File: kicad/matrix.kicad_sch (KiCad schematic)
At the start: 88 parts, among them SW1 Esc, SW10 F9, SW100 Down, SW101 Right, SW11 F10, SW12 F11, SW13 F12, SW14 PrintScreen, SW15 ScrollLock, SW16 PauseBreak, SW18 1, SW19 2, SW2 F1, SW20 3, SW21 4, SW22 5, SW23 6, SW24 7, SW25 8, SW26 9, SW27 0, SW28 -, SW29 =, SW3 F2, SW30 Backspace, SW31 Backspace, SW32 Insert, SW33 Home, SW34 PgUp, SW35 Tab, SW36 Q, SW37 W, SW38 E, SW39 R, SW4 F3, SW40 T, SW41 Y, SW42 U, SW43 I, SW44 O, SW45 P, SW46 [, SW47 ], SW48 \, SW5 F4, SW50 Delete, SW51 End, SW52 PgDw, SW53 CapsLock, SW54 A, SW55 S, SW56 D, SW57 F, SW58 G, SW59 H, SW6 F5, SW60 J, SW61 K, SW62 L, SW63 ;, SW64 ', SW65 \ ISO, SW66 Enter, SW68 Shift, SW69 \ ISO, SW7 F6, SW70 Z, SW71 X, SW72 C, SW73 V, SW74 B, SW75 N, SW76 M, SW77 ,, SW78 ., SW79 /, SW8 F7, SW80 Shift (???), SW81 Shift, SW83 Up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

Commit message: matrix update
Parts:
- added D1, D10, D11, D12, D13, D14, D15, D16, D17, D18, D19, D2, D20, D21, D22, D23, D24, D25, D26, D27, D28, D29, D3, D30, D31, D32, D33, D34, D35, D36, D37, D38, D39, D4, D40, D41, D42, D43, D44, D45, D46, D47, D48, D49, D5, D50, D51, D52, D53, D54, D55, D56, D57, D58, D59, D6, D60, D61, D62, D63, D64, D65, D66, D67, D68, D69, D7, D70, D71, D72, D73, D74, D75, D76, D77, D78, D79, D8, D80, D81, D82, D83, D84, D85, D86, D87, D9: D_Small_Filled, symbol Device:D_Small_Filled
- SW65: renamed from SW68; value Shift -> LShift
- SW77: renamed from SW80; value Shift (???) -> RShift (???)
- SW78: renamed from SW81; value Shift -> RShift
- renumbered SW31 to SW30-1, SW32 to SW31, SW33 to SW32, SW34 to SW33, SW35 to SW34, SW36 to SW35, SW37 to SW36, SW38 to SW37, SW39 to SW38, SW40 to SW39, SW41 to SW40, SW42 to SW41, SW43 to SW42, SW44 to SW43, SW45 to SW44, SW46 to SW45, SW47 to SW46, SW48 to SW47, SW50 to SW48, SW51 to SW49, SW52 to SW50, SW53 to SW51, SW54 to SW52, SW55 to SW53, SW56 to SW54, SW57 to SW55, SW58 to SW56, SW59 to SW57, SW60 to SW58, SW61 to SW59, SW62 to SW60, SW63 to SW61, SW64 to SW62, SW65 to SW63, SW66 to SW64, SW69 to SW66, SW70 to SW67, SW71 to SW68, SW72 to SW69, SW73 to SW70, SW74 to SW71, SW75 to SW72, SW76 to SW73, SW77 to SW74, SW78 to SW75, SW79 to SW76, SW83 to SW79, SW84 to SW80, SW86 to SW81, SW90 to SW82, SW96 to SW83, SW98 to SW84, SW99 to SW85, SW100 to SW86, SW101 to SW87
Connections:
- net COL0: now also D1.1 (K), D10.1 (K), D11.1 (K), D12.1 (K), D13.1 (K), D14.1 (K), D15.1 (K), D16.1 (K), D2.1 (K), D3.1 (K), D4.1 (K), D5.1 (K), D6.1 (K), D7.1 (K), D8.1 (K), D9.1 (K)
- net COL1: now also D18.1 (K), D19.1 (K), D20.1 (K), D21.1 (K), D22.1 (K), D23.1 (K), D24.1 (K), D25.1 (K), D26.1 (K), D27.1 (K), D28.1 (K), D29.1 (K), D30.1 (K), D31.1 (K), D32.1 (K), D33.1 (K)
- net COL2: now also D34.1 (K), D35.1 (K), D36.1 (K), D37.1 (K), D38.1 (K), D39.1 (K), D40.1 (K), D41.1 (K), D42.1 (K), D43.1 (K), D44.1 (K), D45.1 (K), D46.1 (K), D47.1 (K), D48.1 (K), D49.1 (K), D50.1 (K)
- net COL3: now also D51.1 (K), D52.1 (K), D53.1 (K), D54.1 (K), D55.1 (K), D56.1 (K), D57.1 (K), D58.1 (K), D59.1 (K), D60.1 (K), D61.1 (K), D62.1 (K), D63.1 (K)
- net COL4: now also D65.1 (K), D66.1 (K), D67.1 (K), D68.1 (K), D69.1 (K), D70.1 (K), D71.1 (K), D72.1 (K), D73.1 (K), D74.1 (K), D75.1 (K), D76.1 (K), D77.1 (K), D78.1 (K), D79.1 (K)
- net COL5: now also D80.1 (K), D81.1 (K), D82.1 (K), D83.1 (K), D84.1 (K), D85.1 (K), D86.1 (K), D87.1 (K)
- net at SW85.1: now also D85.2 (A)
- net at SW14.1: now also D14.2 (A)
- net at SW16.1: now also D16.2 (A)
- net at SW80.1: now also D80.2 (A)
- net at SW24.1: now also D24.2 (A)
- net at SW20.1: now also D21.2 (A)
- net at SW15.1: now also D15.2 (A)
- net at SW44.1: now also D44.2 (A)
- net at SW42.1: now also D42.2 (A)
- net at SW68.1: now also D68.2 (A)
- net at SW81.1: now also D81.2 (A)
- net at SW70.1: now also D70.2 (A)
- net at SW34.1: now also D34.2 (A)
- net at SW41.1: now also D41.2 (A)
- net at SW43.1: now also D43.2 (A)
- net at SW67.1: now also D67.2 (A)
- net at SW52.1: now also D52.2 (A)
- net at SW17.1: now also D18.2 (A)
- net at SW45.1: now also D45.2 (A)
- net at SW84.1: now also D84.2 (A)
- net at SW22.1: now also D23.2 (A)
- net at SW72.1: now also D72.2 (A)
- net at SW64.1: now also D63.2 (A)
- net at SW82.1: now also D82.2 (A)
- net at SW32.1: now also D32.2 (A)
- net at SW61.1: now also D60.2 (A)
- net at SW79.1: now also D79.2 (A)
- net at SW57.1: now also D56.2 (A)
- net at SW75.1: now also D75.2 (A)
- net at SW13.1: now also D13.2 (A)
- net at SW33.1: now also D33.2 (A)
- net at SW4.1: now also D4.2 (A)
- net at SW29.1: now also D29.2 (A)
- net at SW55.1: now also D54.2 (A)
- net at SW39.1: now also D39.2 (A)
- net at SW78.1: now also D78.2 (A)
- net at SW36.1: now also D36.2 (A)
- net at SW49.1: now also D49.2 (A)
- net at SW48.1: now also D48.2 (A)
- net at SW31.1: now also D31.2 (A)
- net at SW3.1: now also D3.2 (A)
- net at SW54.1: now also D53.2 (A)
- net at SW9.1: now also D9.2 (A)
- net at SW8.1: now also D8.2 (A)
- net at SW83.1: now also D83.2 (A)
- net at SW63.1: now also D62.2 (A)
- net at SW7.1: now also D7.2 (A)
- net at SW73.1: now also D73.2 (A)
- net at SW40.1: now also D40.2 (A)
- net at SW51.1: now also D51.2 (A)
- net at SW69.1: now also D69.2 (A)
- net at SW59.1: now also D58.2 (A)
- net at SW30-1.1, SW30.1: now also D30.2 (A)
- net at SW12.1: now also D12.2 (A)
- net at SW86.1: now also D86.2 (A)
- net at SW66.1: now also D66.2 (A)
- net at SW56.1: now also D55.2 (A)
- net at SW65.1: now also D65.2 (A)
- net at SW62.1: now also D61.2 (A)
- net at SW71.1: now also D71.2 (A)
- net at SW37.1: now also D37.2 (A)
- net at SW25.1: now also D25.2 (A)
- net at SW27.1: now also D27.2 (A)
- net at SW18.1: now also D19.2 (A)
- net at SW77.1: now also D77.2 (A)
- net at SW26.1: now also D26.2 (A)
- net at SW2.1: now also D2.2 (A)
- net at SW6.1: now also D6.2 (A)
- net at SW21.1: now also D22.2 (A)
- net at SW11.1: now also D11.2 (A)
- net at SW35.1: now also D35.2 (A)
- net at SW76.1: now also D76.2 (A)
- net at SW74.1: now also D74.2 (A)
- net at SW47.1: now also D47.2 (A)
- net at SW38.1: now also D38.2 (A)
- net at SW87.1: now also D87.2 (A)
- net at SW10.1: now also D10.2 (A)
- net at SW46.1: now also D46.2 (A)
- net at SW28.1: now also D28.2 (A)
- net at SW60.1: now also D59.2 (A)
- net at SW1.1: now also D1.2 (A)
- net at SW5.1: now also D5.2 (A)
- net at SW58.1: now also D57.2 (A)
- net at SW19.1: now also D20.2 (A)
- net at SW50.1: now also D50.2 (A)
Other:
- moved on the sheet: SW1, SW10, SW11, SW12, SW13, SW14, SW15, SW16, SW17, SW18, SW19, SW2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

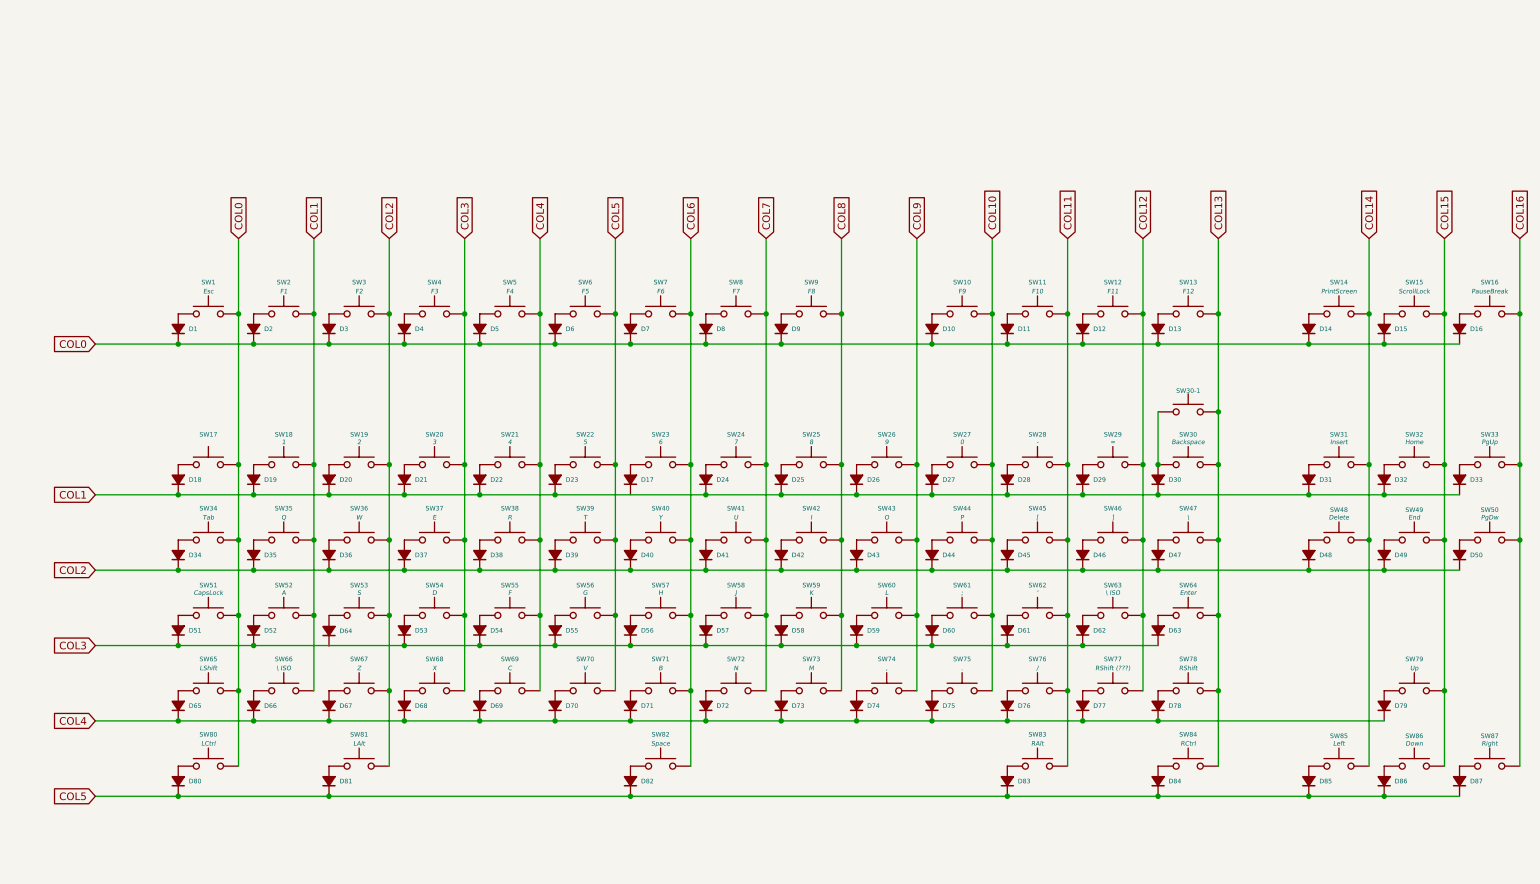
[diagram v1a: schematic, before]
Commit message: Add new symbols to schematic and update selection filter
Added symbols for MCP73831-2-OT, USB_C_Receptacle_USB2.0_14P, R_Small, and MDBT50Q-1MV2 to ibm-modern-m-ssk.kicad_sch. Updated selection filter in ibm-modern-m-ssk.kicad_prl to enable all item types. Removed an old backup zip and renamed a lock file.
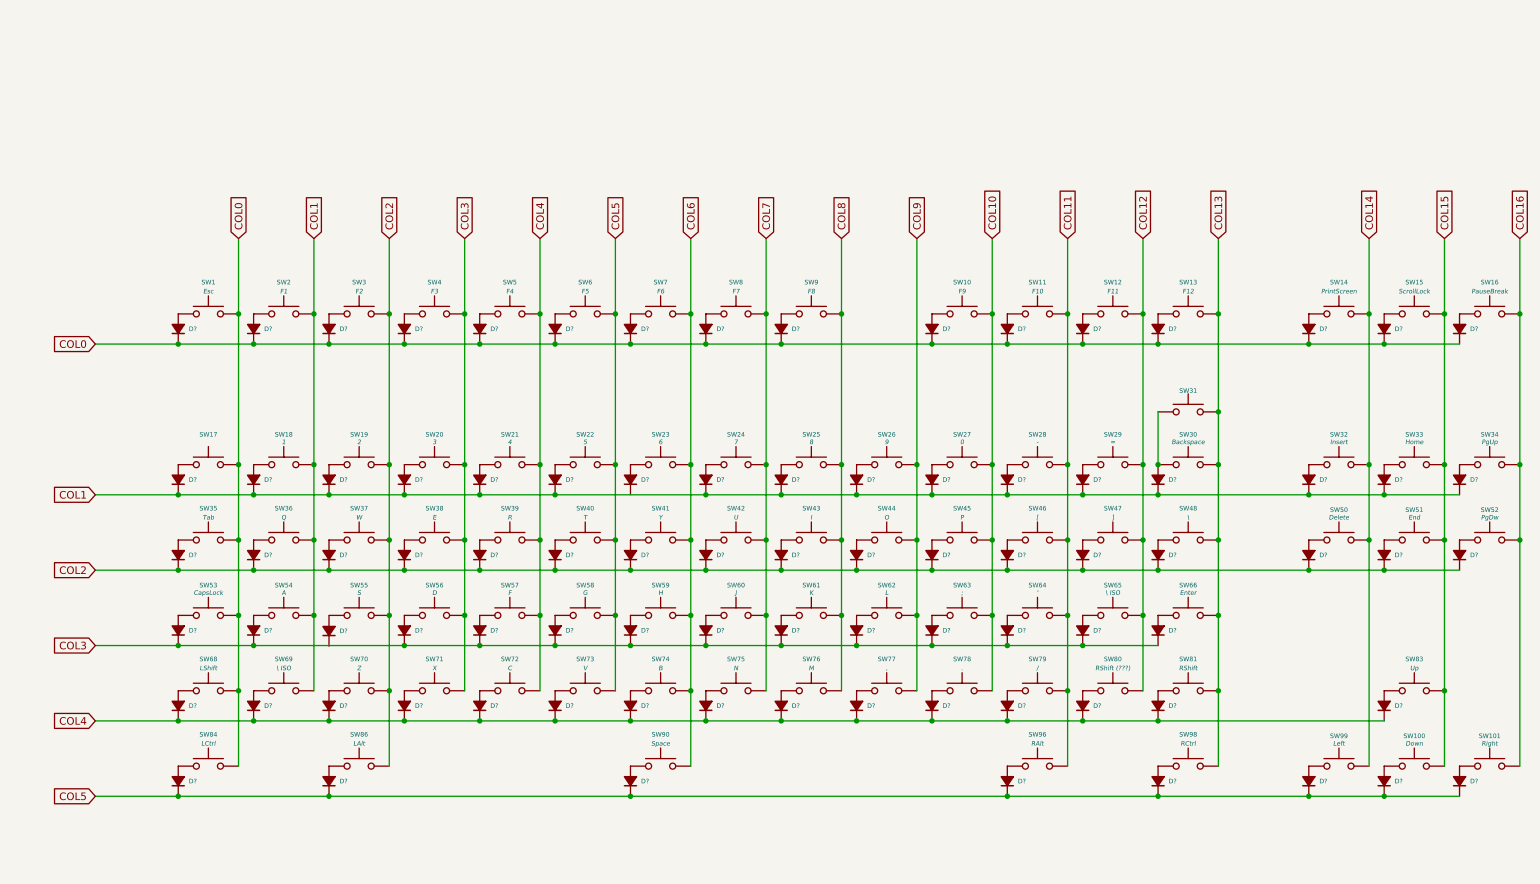
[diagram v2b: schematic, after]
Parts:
- renumbered D6 to D?, D78 to D?, D10 to D?, D32 to D?, D67 to D?, D29 to D?, D33 to D?, D25 to D?, D23 to D?, D11 to D?, D51 to D?, D5 to D?, D9 to D?, D41 to D?, D52 to D?, D59 to D?, D48 to D?, D87 to D?, D22 to D?, D12 to D?, D35 to D?, D4 to D?, D64 to D?, D81 to D?, D8 to D?, D43 to D?, D56 to D?, D54 to D?, D13 to D?, D77 to D?, D16 to D?, D47 to D?, D70 to D?, D20 to D?, D76 to D?, D36 to D?, D85 to D?, D38 to D?, D7 to D?, D80 to D?, D39 to D?, D58 to D?, D50 to D?, D73 to D?, D18 to D?, D31 to D?, D30 to D?, D44 to D?, D63 to D?, D26 to D?, D46 to D?, D17 to D?, D55 to D?, D74 to D?, D28 to D?, D45 to D?, D79 to D?, D37 to D?, D71 to D?, D49 to D?, D66 to D?, D83 to D?, D27 to D?, D68 to D?, D34 to D?, D57 to D?, D24 to D?, D72 to D?, D1 to D?, D19 to D?, D61 to D?, D53 to D?, D42 to D?, D65 to D?, D69 to D?, D15 to D?, D62 to D?, D82 to D?, D2 to D?, D75 to D?, D86 to D?, D84 to D?, D14 to D?, D40 to D?, D3 to D?, D60 to D?, D21 to D?, SW86 to SW100, SW87 to SW101, SW30-1 to SW31, SW31 to SW32, SW32 to SW33, SW33 to SW34, SW34 to SW35, SW35 to SW36, SW36 to SW37, SW37 to SW38, SW38 to SW39, SW39 to SW40, SW40 to SW41, SW41 to SW42, SW42 to SW43, SW43 to SW44, SW44 to SW45, SW45 to SW46, SW46 to SW47, SW47 to SW48, SW48 to SW50, SW49 to SW51, SW50 to SW52, SW51 to SW53, SW52 to SW54, SW53 to SW55, SW54 to SW56, SW55 to SW57, SW56 to SW58, SW57 to SW59, SW58 to SW60, SW59 to SW61, SW60 to SW62, SW61 to SW63, SW62 to SW64, SW63 to SW65, SW64 to SW66, SW65 to SW68, SW66 to SW69, SW67 to SW70, SW68 to SW71, SW69 to SW72, SW70 to SW73, SW71 to SW74, SW72 to SW75, SW73 to SW76, SW74 to SW77, SW75 to SW78, SW76 to SW79, SW77 to SW80, SW78 to SW81, SW79 to SW83, SW80 to SW84, SW81 to SW86, SW82 to SW90, SW83 to SW96, SW84 to SW98, SW85 to SW99

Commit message: Schematic Done v2
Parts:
- D10, D11, D12, D13, D14, D15, D16, D17, D18, D19, D20, D21, D22, D23, D24, D25, D26, D27, D28, D29, D30, D31, D32, D33, D34, D35, D36, D37, D38, D39, D40, D41, D42, D43, D44, D45, D46, D47, D48, D49, D5, D50, D51, D52, D53, D54, D55, D56, D57, D58, D59, D6, D60, D61, D62, D63, D64, D65, D66, D67, D68, D69, D7, D70, D71, D72, D73, D74, D75, D76, D77, D78, D79, D8, D80, D81, D82, D83, D84, D85, D86, D87, D88, D89, D9, D90, D91: renamed from D?; symbol Device:D_Small_Filled -> Device:D_Small
- renumbered SW31 to SW17, SW17 to SW18, SW18 to SW19, SW19 to SW20, SW20 to SW21, SW21 to SW22, SW22 to SW23, SW23 to SW24, SW24 to SW25, SW25 to SW26, SW26 to SW27, SW27 to SW28, SW28 to SW29, SW29 to SW30, SW30 to SW31, SW50 to SW49, SW51 to SW50, SW52 to SW51, SW53 to SW52, SW54 to SW53, SW55 to SW54, SW56 to SW55, SW57 to SW56, SW58 to SW57, SW59 to SW58, SW60 to SW59, SW61 to SW60, SW62 to SW61, SW63 to SW62, SW64 to SW63, SW65 to SW64, SW66 to SW65, SW68 to SW66, SW69 to SW67, SW70 to SW68, SW71 to SW69, SW72 to SW70, SW73 to SW71, SW74 to SW72, SW75 to SW73, SW76 to SW74, SW77 to SW75, SW78 to SW76, SW79 to SW77, SW80 to SW78, SW81 to SW79, SW83 to SW80, SW84 to SW81, SW86 to SW82, SW90 to SW83, SW96 to SW84, SW98 to SW85, SW99 to SW86, SW100 to SW87, SW101 to SW88

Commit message: Footprints & BOM done
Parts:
- D10, D11, D12, D13, D14, D15, D16, D17, D18, D19, D20, D21, D22, D23, D24, D25, D26, D27, D28, D29, D30, D31, D32, D33, D34, D35, D36, D37, D38, D39, D40, D41, D42, D43, D44, D45, D46, D47, D48, D49, D5, D50, D51, D52, D53, D54, D55, D56, D57, D58, D59, D6, D60, D61, D62, D63, D64, D65, D66, D67, D68, D69, D7, D70, D71, D72, D73, D74, D75, D76, D77, D78, D79, D8, D80, D81, D82, D83, D84, D85, D86, D87, D88, D89, D9, D90, D91: footprint (none) -> easyeda2kicad:SOD-723_L1.0-W0.6-P1.4-RD; LCSC Part (none) -> C2288
- SW1, SW10, SW11, SW12, SW13, SW14, SW15, SW16, SW17, SW18, SW19, SW2, SW20, SW21, SW22, SW23, SW24, SW25, SW26, SW27, SW28, SW29, SW3, SW30, SW31, SW32, SW33, SW34, SW35, SW36, SW37, SW38, SW39, SW4, SW40, SW41, SW42, SW43, SW44, SW45, SW46, SW47, SW48, SW49, SW5, SW50, SW51, SW52, SW53, SW54, SW55, SW56, SW57, SW58, SW59, SW6, SW60, SW61, SW62, SW63, SW64, SW65, SW66, SW67, SW68, SW69, SW7, SW70, SW71, SW72, SW73, SW74, SW75, SW76, SW77, SW78, SW79, SW8, SW80, SW81, SW82, SW83, SW84, SW85, SW86, SW87, SW88, SW9: footprint (none) -> ibm_bs:ibm_bs_1u; now left out of the parts list

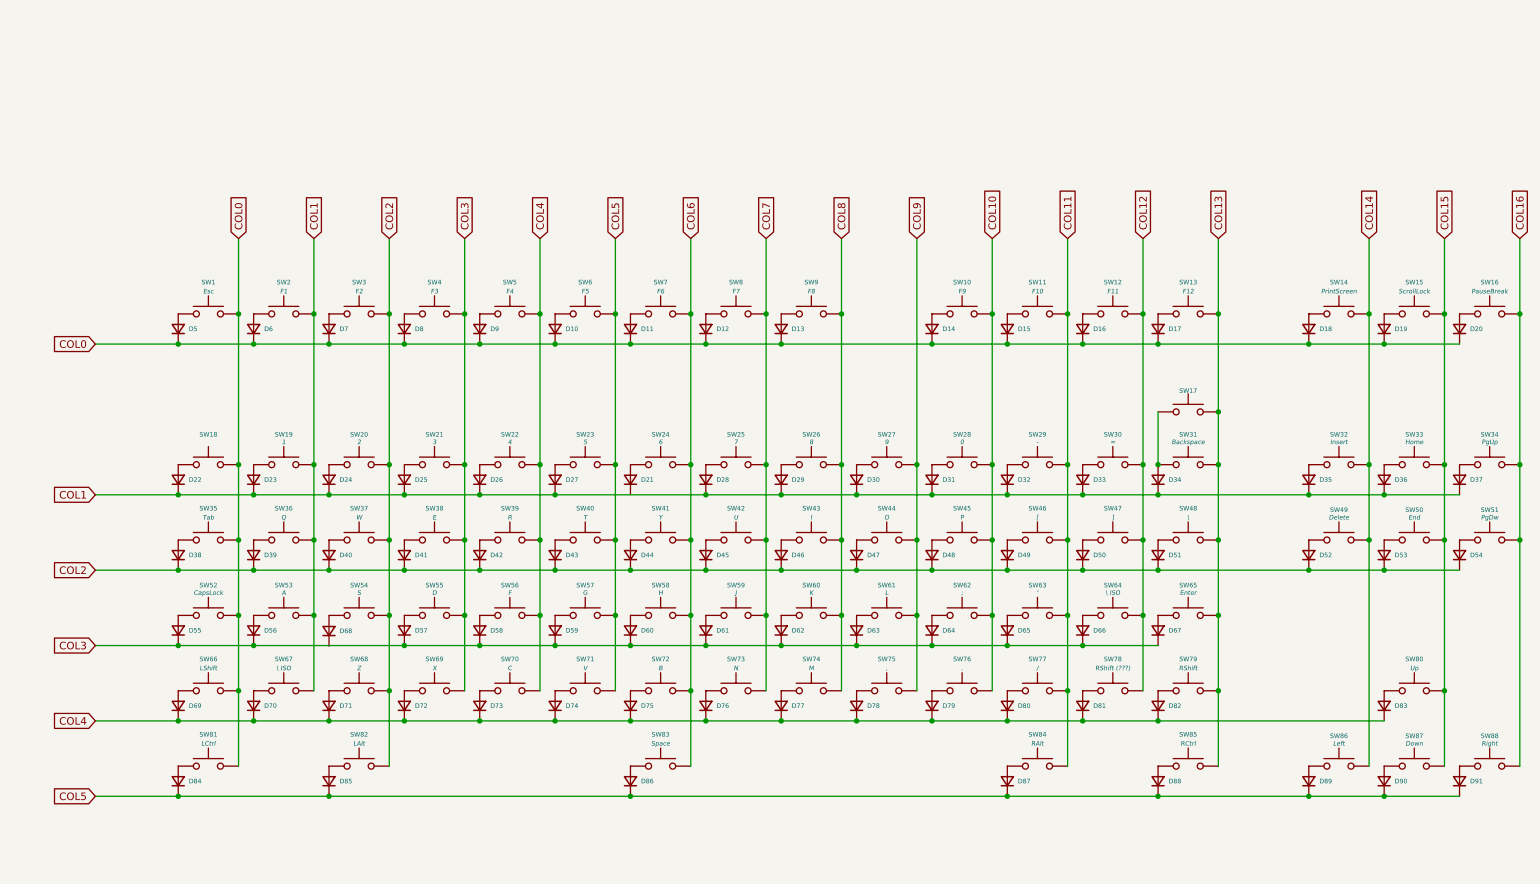
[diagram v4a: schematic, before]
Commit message: Update KiCad schematic, project files and backups
Rotate backups, and adjust KiCad project/schematic files. Deleted kicad/#auto_saved_files# and removed an old backup; added two new ibm-modern-m-ssk backup zips. Updated kicad/ibm-modern-m-ssk.kicad_prl and .kicad_pro (visible items/layers and meta/version changes, and removal of a netclass priority). Large edits to kicad/matrix.kicad_sch: added FPC connector symbol (TF38-24S-0.5SV), updated many component/junction coordinates and symbol details (likely placement/layout changes or library imports). Also renamed a .lck entry. These changes reflect schematic updates and housekeeping for project backups.
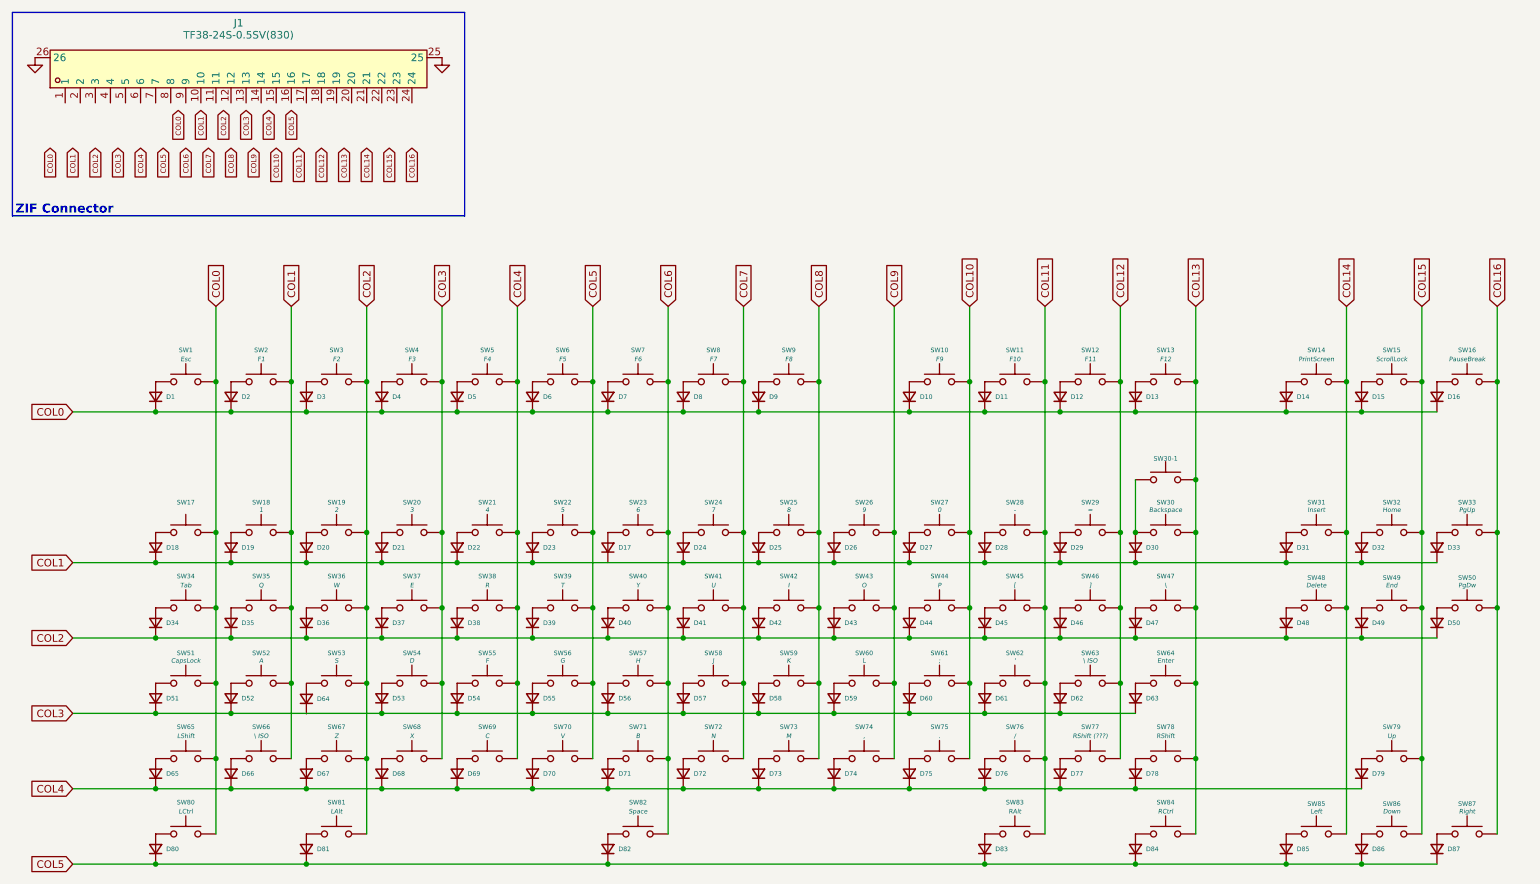
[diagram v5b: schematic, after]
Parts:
- added J1: TF38-24S-0.5SV(830), easyeda2kicad:FPC-SMD_24P-P0.50_TF38-24S-0.5SV-830, symbol easyeda2kicad:TF38-24S-0.5SV(830)
- renumbered D5 to D1, D14 to D10, D15 to D11, D16 to D12, D17 to D13, D18 to D14, D19 to D15, D20 to D16, D21 to D17, D22 to D18, D23 to D19, D6 to D2, D24 to D20, D25 to D21, D26 to D22, D27 to D23, D28 to D24, D29 to D25, D30 to D26, D31 to D27, D32 to D28, D33 to D29, D7 to D3, D34 to D30, D35 to D31, D36 to D32, D37 to D33, D38 to D34, D39 to D35, D40 to D36, D41 to D37, D42 to D38, D43 to D39, D8 to D4, D44 to D40, D45 to D41, D46 to D42, D47 to D43, D48 to D44, D49 to D45, D50 to D46, D51 to D47, D52 to D48, D53 to D49, D9 to D5, D54 to D50, D55 to D51, D56 to D52, D57 to D53, D58 to D54, D59 to D55, D60 to D56, D61 to D57, D62 to D58, D63 to D59, D10 to D6, D64 to D60, D65 to D61, D66 to D62, D67 to D63, D68 to D64, D69 to D65, D70 to D66, D71 to D67, D72 to D68, D73 to D69, D11 to D7, D74 to D70, D75 to D71, D76 to D72, D77 to D73, D78 to D74, D79 to D75, D80 to D76, D81 to D77, D82 to D78, D83 to D79, D12 to D8, D84 to D80, D85 to D81, D86 to D82, D87 to D83, D88 to D84, D89 to D85, D90 to D86, D91 to D87, D13 to D9, SW18 to SW17, SW19 to SW18, SW20 to SW19, SW21 to SW20, SW22 to SW21, SW23 to SW22, SW24 to SW23, SW25 to SW24, SW26 to SW25, SW27 to SW26, SW28 to SW27, SW29 to SW28, SW30 to SW29, SW31 to SW30, SW17 to SW30-1, SW32 to SW31, SW33 to SW32, SW34 to SW33, SW35 to SW34, SW36 to SW35, SW37 to SW36, SW38 to SW37, SW39 to SW38, SW40 to SW39, SW41 to SW40, SW42 to SW41, SW43 to SW42, SW44 to SW43, SW45 to SW44, SW46 to SW45, SW47 to SW46, SW48 to SW47, SW49 to SW48, SW50 to SW49, SW51 to SW50, SW52 to SW51, SW53 to SW52, SW54 to SW53, SW55 to SW54, SW56 to SW55, SW57 to SW56, SW58 to SW57, SW59 to SW58, SW60 to SW59, SW61 to SW60, SW62 to SW61, SW63 to SW62, SW64 to SW63, SW65 to SW64, SW66 to SW65, SW67 to SW66, SW68 to SW67, SW69 to SW68, SW70 to SW69, SW71 to SW70, SW72 to SW71, SW73 to SW72, SW74 to SW73, SW75 to SW74, SW76 to SW75, SW77 to SW76, SW78 to SW77, SW79 to SW78, SW80 to SW79, SW81 to SW80, SW82 to SW81, SW83 to SW82, SW84 to SW83, SW85 to SW84, SW86 to SW85, SW87 to SW86, SW88 to SW87
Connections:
- new net GND: J1.25, J1.26
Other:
- note added: "ZIF Connector"
- moved on the sheet: D1, D10, D11, D12, D13, D14, D15, D16, D17, D18, D19, D2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

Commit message: Add LiPo STEP/module and backups, update schematic
Add LiPo_603450_1200mAh STEP (3D) and corresponding .kicad_mod to the easyeda2kicad libraries, add two ibm-modern-m-ssk backup ZIPs, and update kicad/matrix.kicad_sch. Remove stale PCB lock file (~ibm-modern-m-ssk.kicad_pcb.lck). These changes introduce a battery 3D model/module and include recent project backups while applying a schematic update.
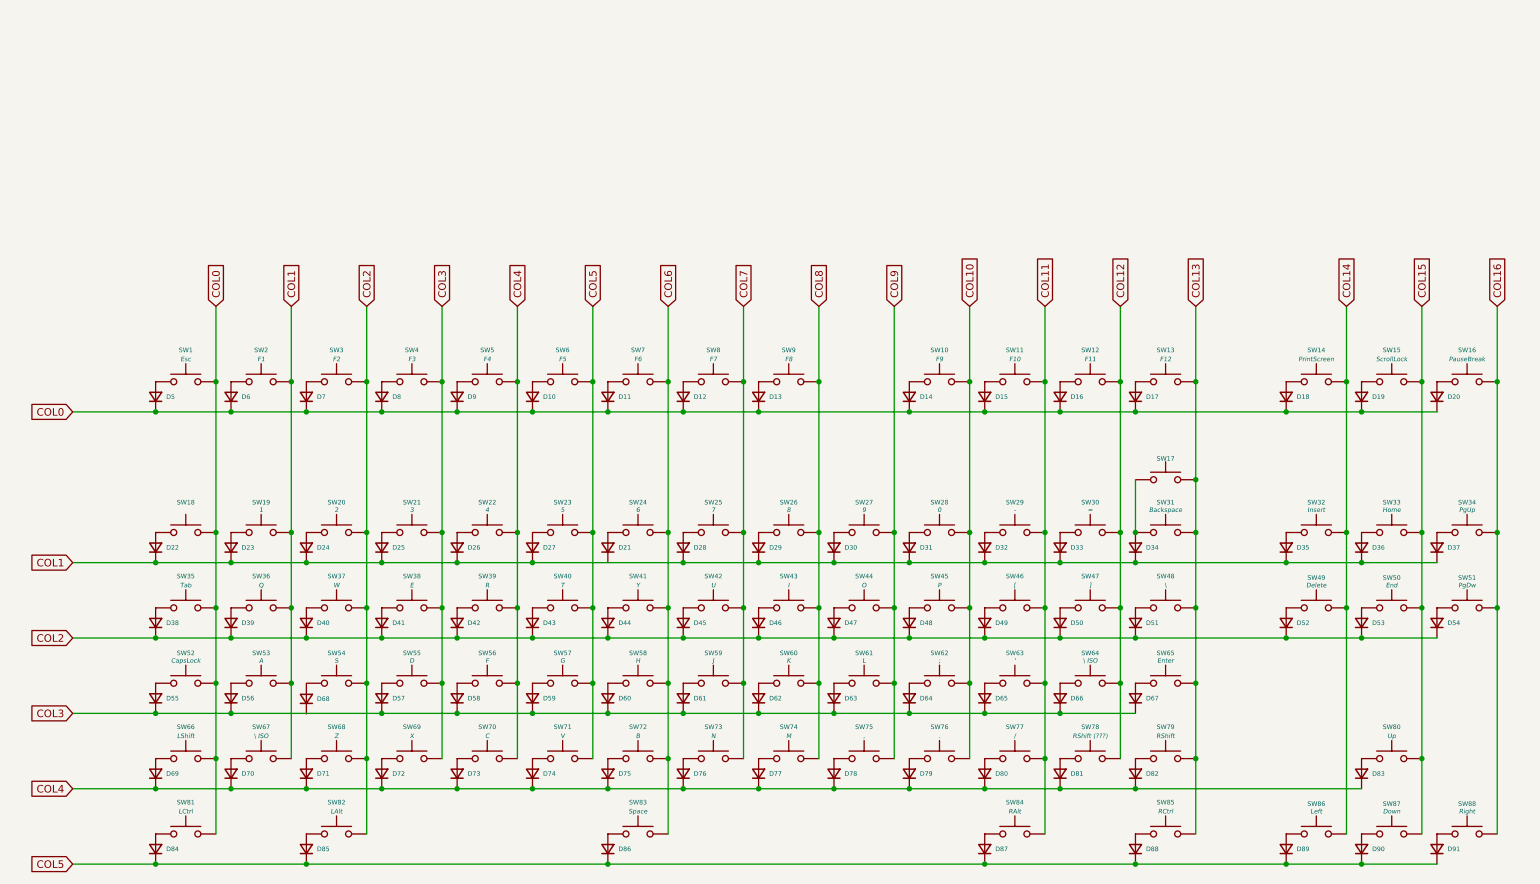
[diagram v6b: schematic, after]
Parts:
- removed J1: TF38-24S-0.5SV(830), easyeda2kicad:FPC-SMD_24P-P0.50_TF38-24S-0.5SV-830, symbol easyeda2kicad:TF38-24S-0.5SV(830)
- renumbered D6 to D10, D7 to D11, D8 to D12, D9 to D13, D10 to D14, D11 to D15, D12 to D16, D13 to D17, D14 to D18, D15 to D19, D16 to D20, D17 to D21, D18 to D22, D19 to D23, D20 to D24, D21 to D25, D22 to D26, D23 to D27, D24 to D28, D25 to D29, D26 to D30, D27 to D31, D28 to D32, D29 to D33, D30 to D34, D31 to D35, D32 to D36, D33 to D37, D34 to D38, D35 to D39, D36 to D40, D37 to D41, D38 to D42, D39 to D43, D40 to D44, D41 to D45, D42 to D46, D43 to D47, D44 to D48, D45 to D49, D1 to D5, D46 to D50, D47 to D51, D48 to D52, D49 to D53, D50 to D54, D51 to D55, D52 to D56, D53 to D57, D54 to D58, D55 to D59, D2 to D6, D56 to D60, D57 to D61, D58 to D62, D59 to D63, D60 to D64, D61 to D65, D62 to D66, D63 to D67, D64 to D68, D65 to D69, D3 to D7, D66 to D70, D67 to D71, D68 to D72, D69 to D73, D70 to D74, D71 to D75, D72 to D76, D73 to D77, D74 to D78, D75 to D79, D4 to D8, D76 to D80, D77 to D81, D78 to D82, D79 to D83, D80 to D84, D81 to D85, D82 to D86, D83 to D87, D84 to D88, D85 to D89, D5 to D9, D86 to D90, D87 to D91, SW30-1 to SW17, SW17 to SW18, SW18 to SW19, SW19 to SW20, SW20 to SW21, SW21 to SW22, SW22 to SW23, SW23 to SW24, SW24 to SW25, SW25 to SW26, SW26 to SW27, SW27 to SW28, SW28 to SW29, SW29 to SW30, SW30 to SW31, SW31 to SW32, SW32 to SW33, SW33 to SW34, SW34 to SW35, SW35 to SW36, SW36 to SW37, SW37 to SW38, SW38 to SW39, SW39 to SW40, SW40 to SW41, SW41 to SW42, SW42 to SW43, SW43 to SW44, SW44 to SW45, SW45 to SW46, SW46 to SW47, SW47 to SW48, SW48 to SW49, SW49 to SW50, SW50 to SW51, SW51 to SW52, SW52 to SW53, SW53 to SW54, SW54 to SW55, SW55 to SW56, SW56 to SW57, SW57 to SW58, SW58 to SW59, SW59 to SW60, SW60 to SW61, SW61 to SW62, SW62 to SW63, SW63 to SW64, SW64 to SW65, SW65 to SW66, SW66 to SW67, SW67 to SW68, SW68 to SW69, SW69 to SW70, SW70 to SW71, SW71 to SW72, SW72 to SW73, SW73 to SW74, SW74 to SW75, SW75 to SW76, SW76 to SW77, SW77 to SW78, SW78 to SW79, SW79 to SW80, SW80 to SW81, SW81 to SW82, SW82 to SW83, SW83 to SW84, SW84 to SW85, SW85 to SW86, SW86 to SW87, SW87 to SW88
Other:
- note removed: "ZIF Connector"

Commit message: update
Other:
- moved on the sheet: D10, D11, D12, D13, D14, D15, D16, D17, D18, D19, D20, D21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
